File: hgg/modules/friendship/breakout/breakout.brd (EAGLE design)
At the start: 91 x 29.5 mm, 7 parts, among them IC1 MAX481CSA, IC2 MAX481CSA

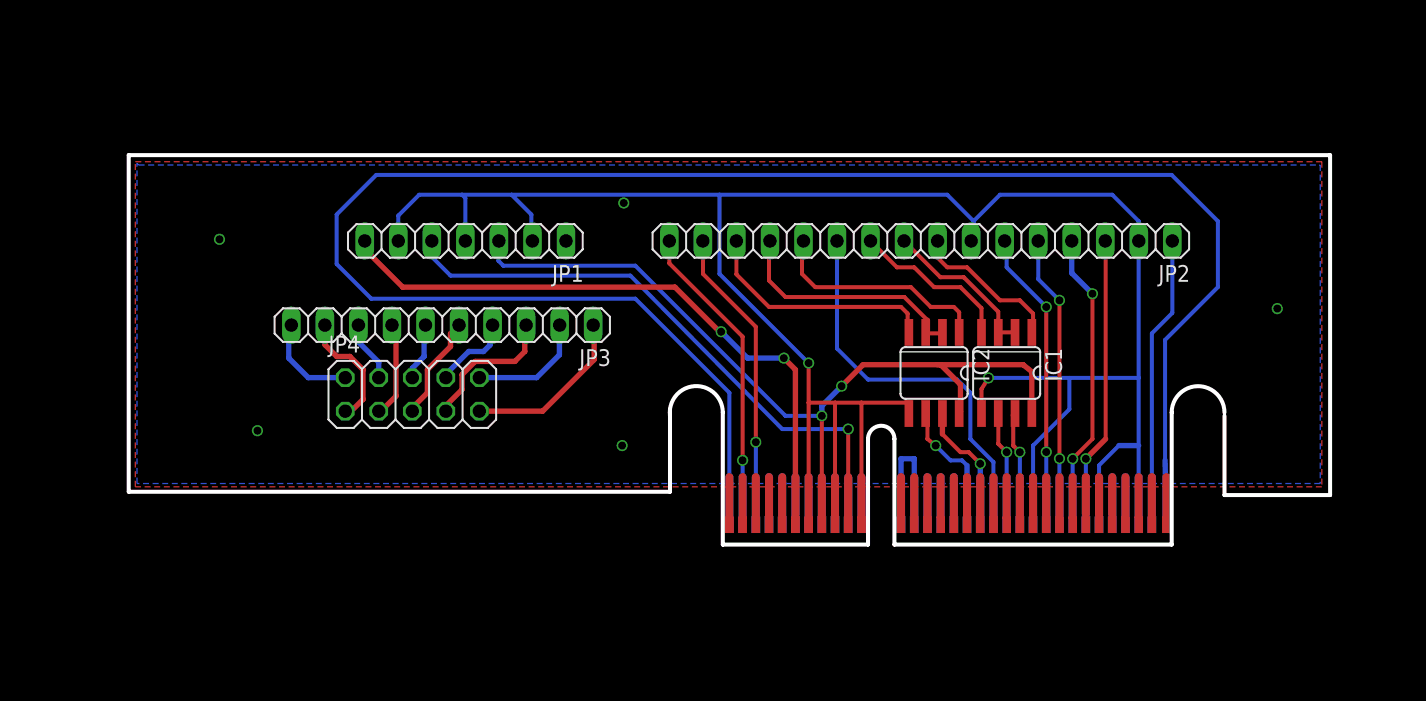
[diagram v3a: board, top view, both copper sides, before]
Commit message: changed breakout to use full busmaster plug port
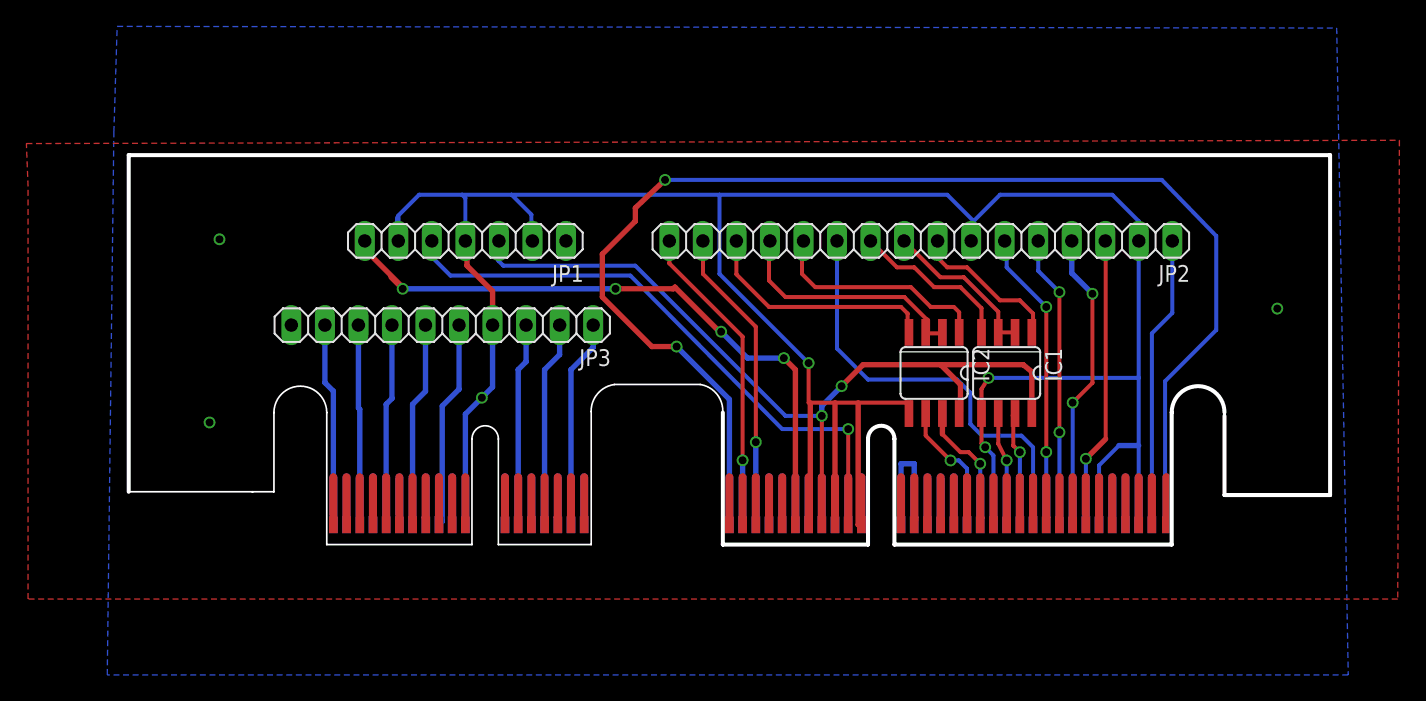
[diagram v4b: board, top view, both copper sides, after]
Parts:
- removed JP4: (no value), pinhead:2X05
- U$1: value FRIENDSHIPCONNECTOR -> BUSMASTER; device hgg:FRIENDSHIP_EDGE_CONNECTOR -> hgg:BUSMASTER_EDGE_CONNECTOR
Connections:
- removed net N$24: JP3.9, JP4.1
- removed net N$30: JP3.4, JP4.8
- removed net N$31: JP3.2, JP4.10
- removed net N$32: JP3.1, JP4.9
- new net N$13: JP3.1, U$1.BMB17(IRQ/PRSNT_CLK)
- new net N$18: JP3.2, U$1.BMB15(SH/LD_PRSNT/IRQ)
- net GND: now also JP3.4, U$1.A19(GND), U$1.BMB11(GND); no longer U$1.A22(GND)
- net N$10: now also U$1.A22(GND); no longer U$1.A19(GND)
- net N$22: now also JP3.3, U$1.BMB13(INTACK_SER); no longer JP3.10, JP4.2
- net N$25: now also JP3.5, U$1.BMB09(INTACK_RCK); no longer JP3.8, JP4.4
- net N$26: now also JP3.6, U$1.BMB07(INTACK_SCK); no longer JP3.7, JP4.3
- net N$27: now also JP3.7, U$1.BMB05(PRSNT_DATAIN); no longer JP3.6, JP4.6
- net N$28: now also JP3.8, U$1.BMB03(IRQ); no longer JP3.5, JP4.5
- net N$29: now also JP3.9, U$1.BMB01(IRQ_DATAIN); no longer JP3.3, JP4.7
- net VCC: now also U$1.B08(+5V)
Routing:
- net N$1: track 141.6 -> 100.3 mm, vias 0 -> 2
- net GND: track 182.4 -> 204.9 mm
- net N$13: track 0.00 -> 15.8 mm
- net N$18: track 0.00 -> 15.6 mm
- net N$32: track 13.0 -> 0.00 mm
- net N$25: track 4.63 -> 15.8 mm
- net N$27: track 4.39 -> 15.3 mm
- net N$24: track 9.13 -> 0.00 mm
- net N$31: track 9.04 -> 0.00 mm
- net N$26: track 7.29 -> 15.5 mm
- net N$22: track 7.47 -> 15.4 mm
- net N$28: track 7.99 -> 15.2 mm
- net N$30: track 6.11 -> 0.00 mm
- net N$29: track 10.8 -> 15.4 mm
- net N$10: track 30.4 -> 33.4 mm
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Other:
- outline, holes or cut-outs redrawn

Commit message: applied DRCs, not all passing, minor routing improvements, increased trace width
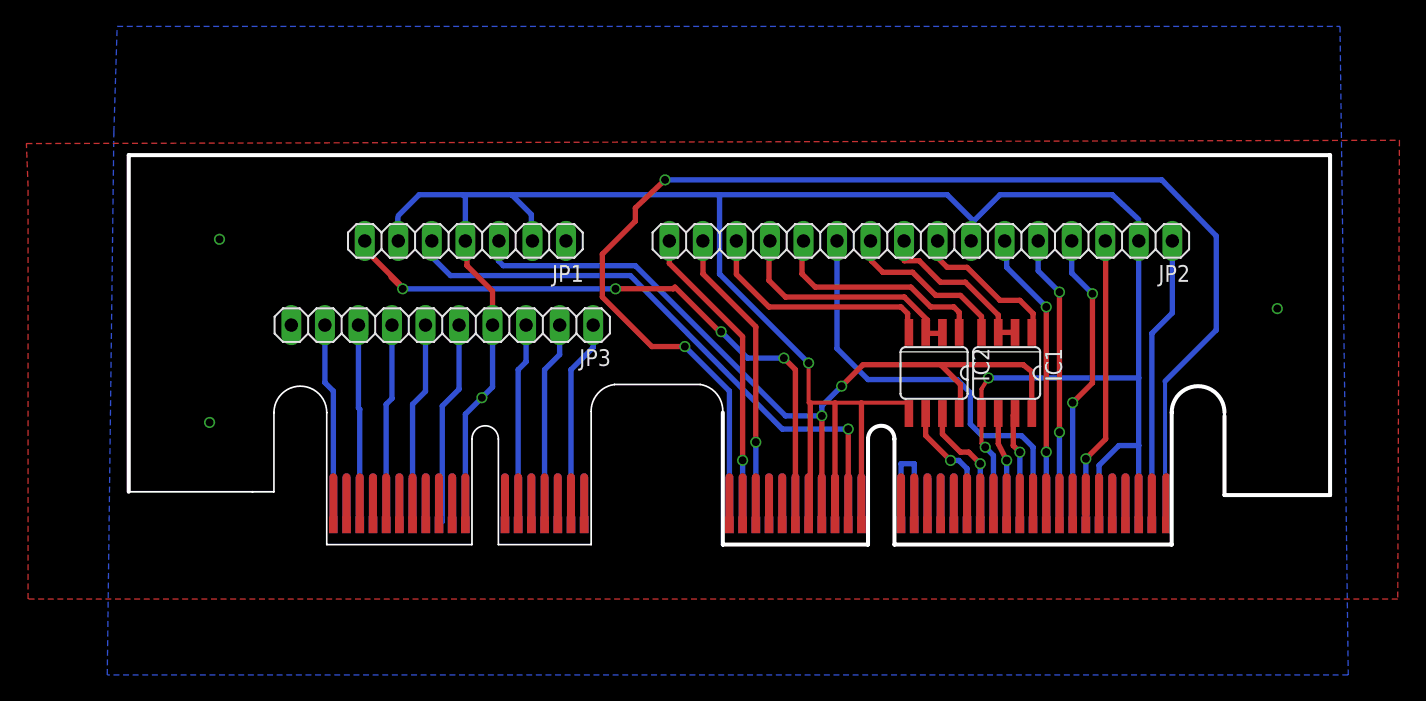
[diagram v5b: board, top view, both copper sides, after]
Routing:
- net N$11: track 12.2 -> 12.9 mm
- net GND: track 204.9 -> 204.7 mm, vias 9 -> 7
